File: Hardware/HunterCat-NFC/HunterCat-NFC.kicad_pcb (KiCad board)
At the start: 2 copper layers, 80.7 x 33.5 mm, 86 parts, among them J1 Battery, P1 USB_C_Plug_USB2.0, Q1 DMG3415U-7, SW1 RESET, SW2 GPIO0, SW3 GPIO1, SW4 GPIO2, SW5 ON, U1 RP2040, U2 PN7150B0HN_C11002E-PN7150B0HN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

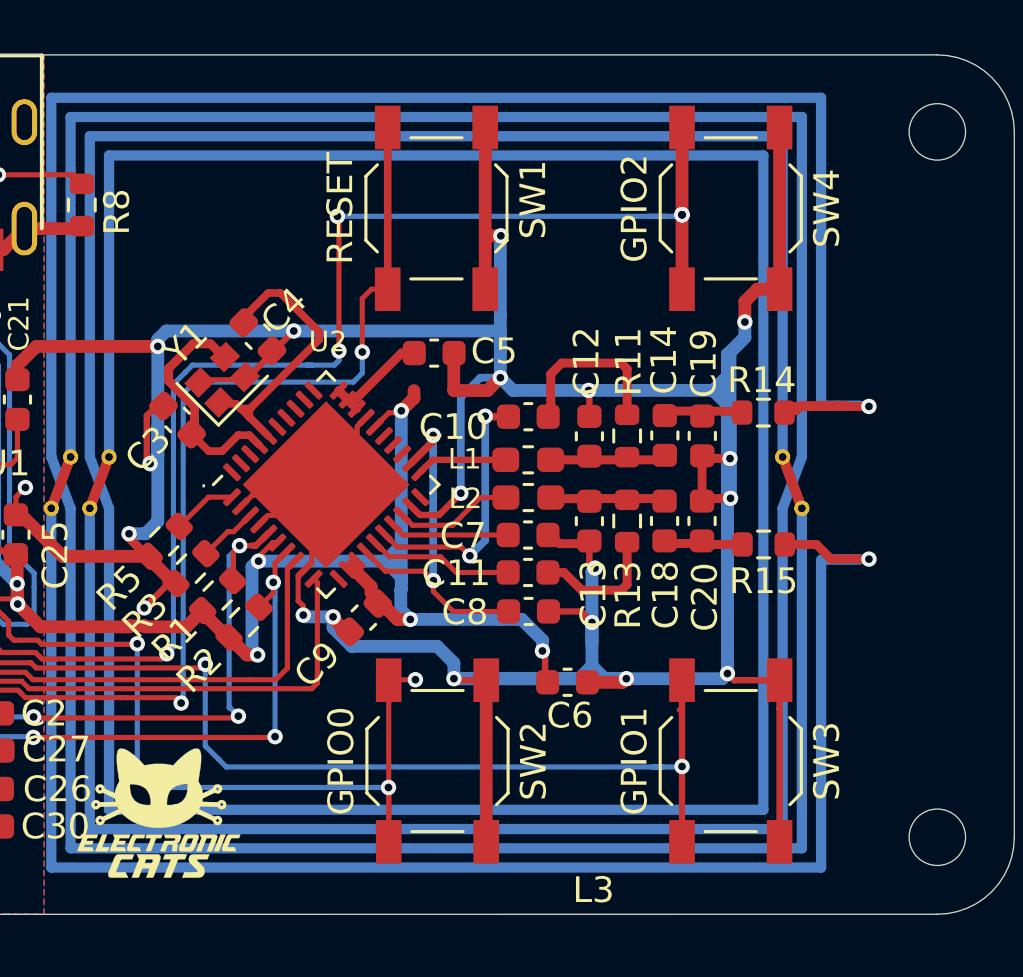
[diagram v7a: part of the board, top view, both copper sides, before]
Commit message: Changed Button
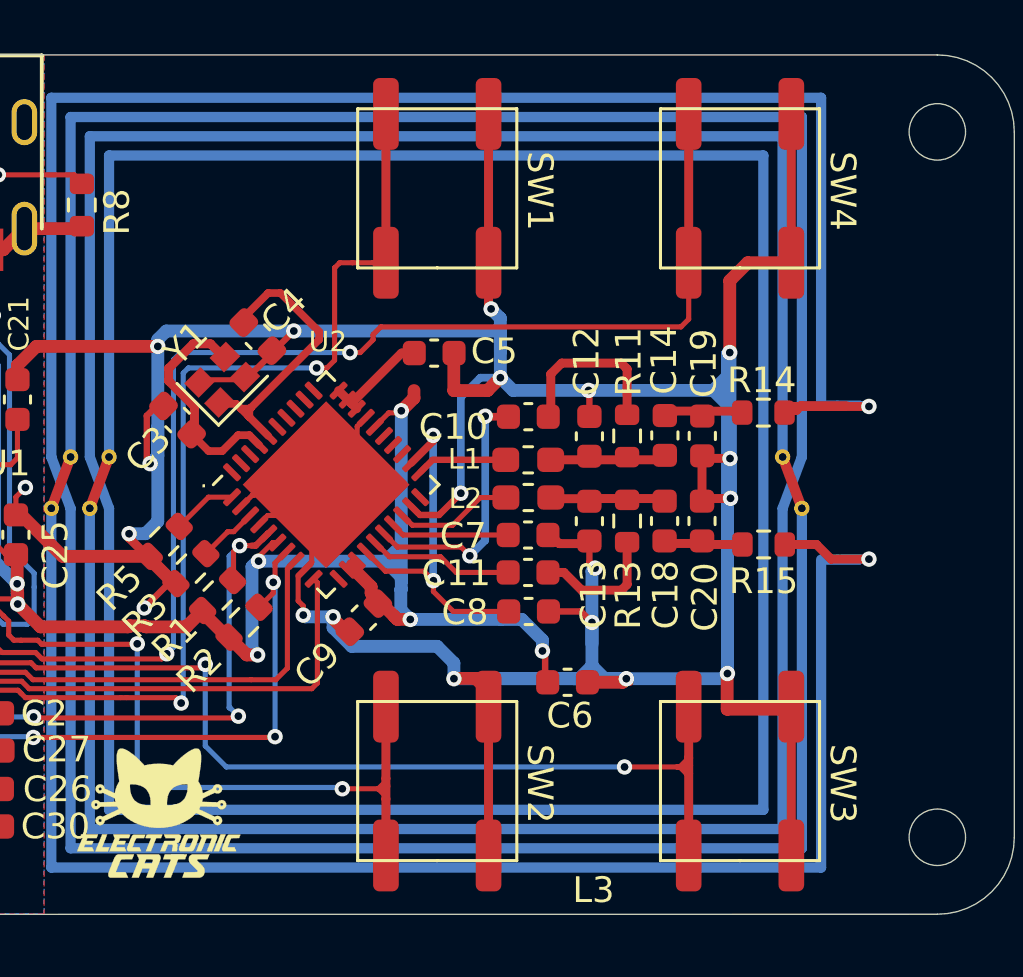
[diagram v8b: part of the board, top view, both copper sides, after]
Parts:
- R10: value 1K -> 4.7K
- SW1, SW3, SW4: footprint Button_Switch_SMD:SW_SPST_TL3342 -> hunter-cat-nfc:KSC941JLFS
- SW2: value GPIO0 -> GPIO; footprint Button_Switch_SMD:SW_SPST_TL3342 -> hunter-cat-nfc:KSC941JLFS
- moved SW3 0.86 mm to (150.0, 103.8)
- moved SW4 0.86 mm to (150.0, 80.7)
- moved SW1 0.78 mm to (138.2, 80.7)
- moved SW2 0.78 mm to (138.2, 103.8)
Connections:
- U1 pad 2: /TX -> unconnected-(U1-Pad2)
- U1 pad 3: /RX -> unconnected-(U1-Pad3)
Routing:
- net GND: track 258.1 -> 250.6 mm
- net /GPIO: track 52.8 -> 49.4 mm, vias 5 -> 2
- net /GPIO1: track 31.0 -> 29.3 mm, vias 3 -> 2
- net /GPIO2: track 40.4 -> 39.6 mm
- net /RST: track 40.7 -> 41.5 mm
